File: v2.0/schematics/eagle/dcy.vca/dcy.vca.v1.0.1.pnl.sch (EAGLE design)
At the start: 21 parts

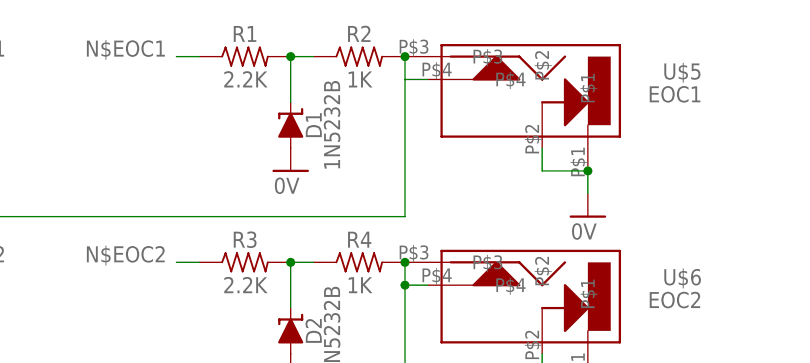
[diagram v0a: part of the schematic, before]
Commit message: Flipped oritentaiton of panel board Changed power header to 2x5 hearder
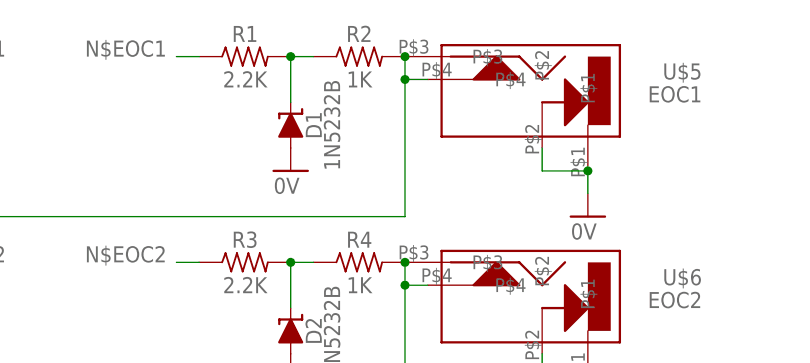
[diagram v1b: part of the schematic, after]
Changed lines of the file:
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@@
 <wire x1="58.42" y1="-5.08" x2="58.42" y2="-20.32" width="0.1524" layer="91"/>
 <wire x1="116.84" y1="-20.32" x2="58.42" y2="-20.32" width="0.1524" layer="91"/>
+<junction x="116.84" y="-5.08"/>
 </segment>
 </net>

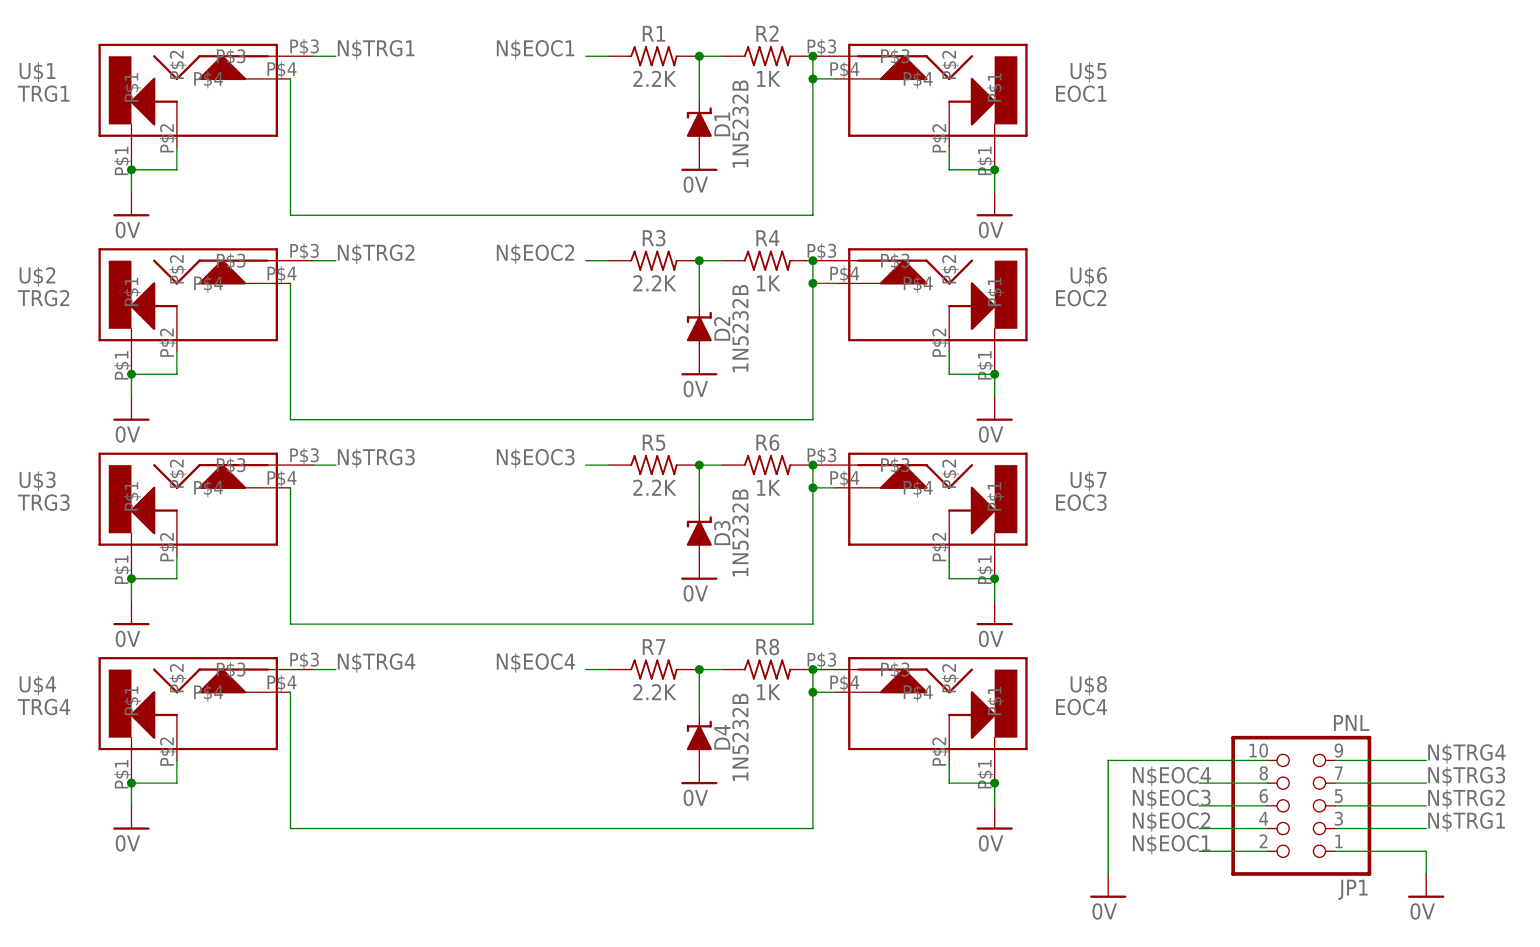
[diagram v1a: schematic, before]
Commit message: Updated routing and jack position.
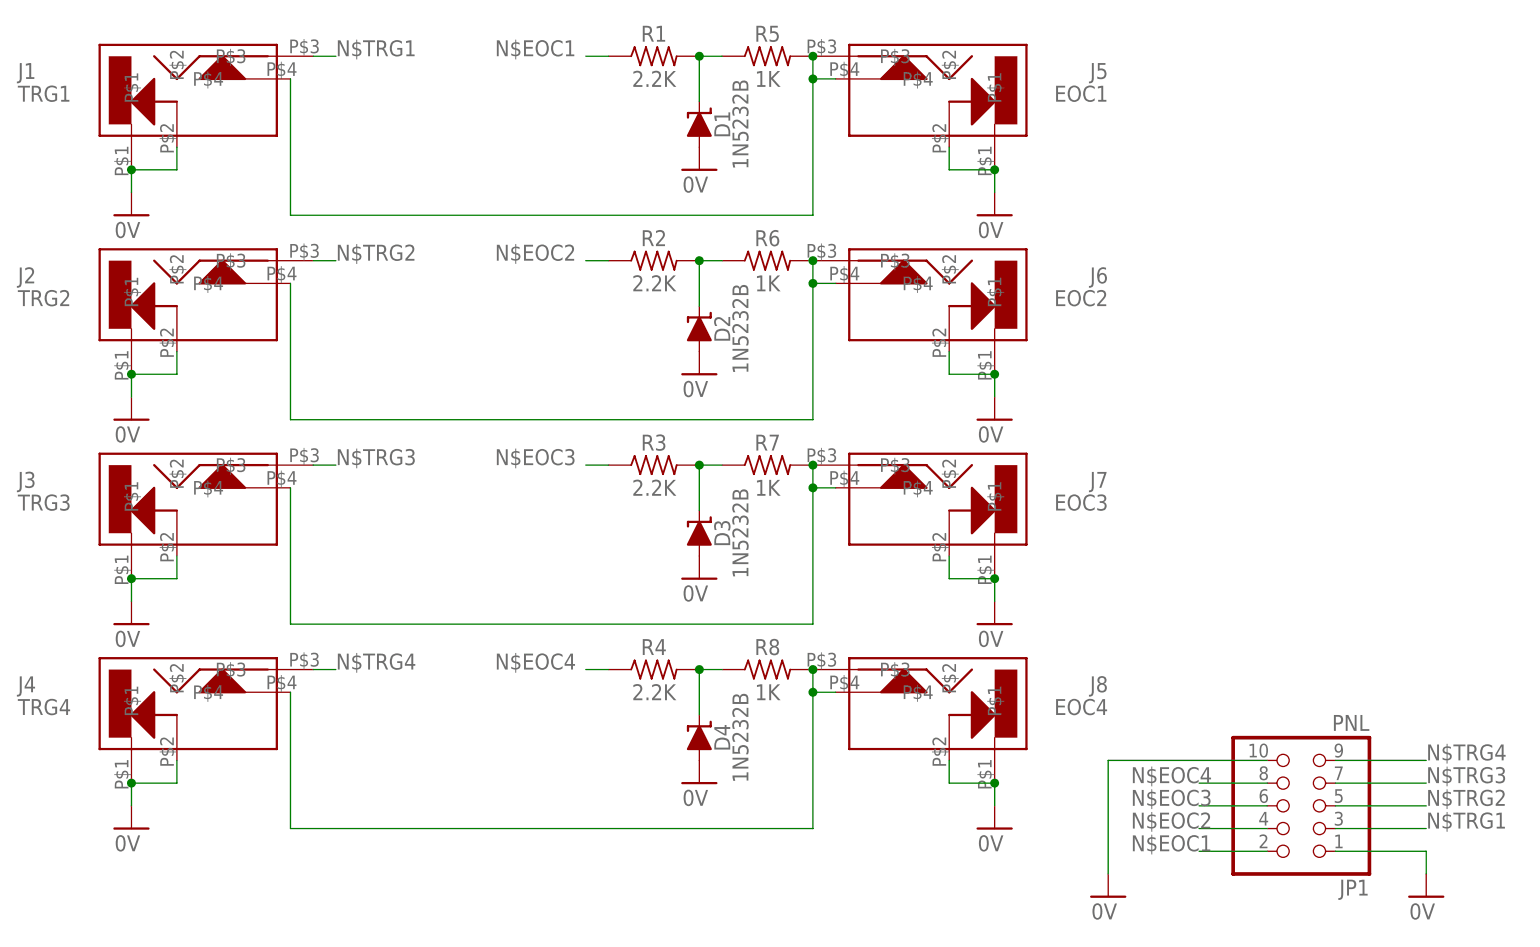
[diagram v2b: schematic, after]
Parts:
- R2, R4: value 1K -> 2.2K
- R5, R7: value 2.2K -> 1K
- renumbered U$1 to J1, U$2 to J2, U$3 to J3, U$4 to J4, U$5 to J5, U$6 to J6, U$7 to J7, U$8 to J8
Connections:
- net N$1: now also R5.1; no longer R2.1
- net N$2: now also R5.2; no longer R2.2
- net N$3: now also R2.2, R6.1; no longer R3.2, R4.1
- net N$4: now also R3.2, R7.1; no longer R5.2, R6.1
- net N$5: now also R4.2; no longer R7.2
- net N$6: now also R6.2; no longer R4.2
- net N$7: now also R7.2; no longer R6.2
- net N$EOC2: now also R2.1; no longer R3.1
- net N$EOC3: now also R3.1; no longer R5.1
- net N$EOC4: now also R4.1; no longer R7.1
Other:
- moved on the sheet: R2, R3, R4, R5, R6, R7
